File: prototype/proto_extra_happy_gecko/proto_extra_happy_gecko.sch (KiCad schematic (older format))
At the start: 0 parts

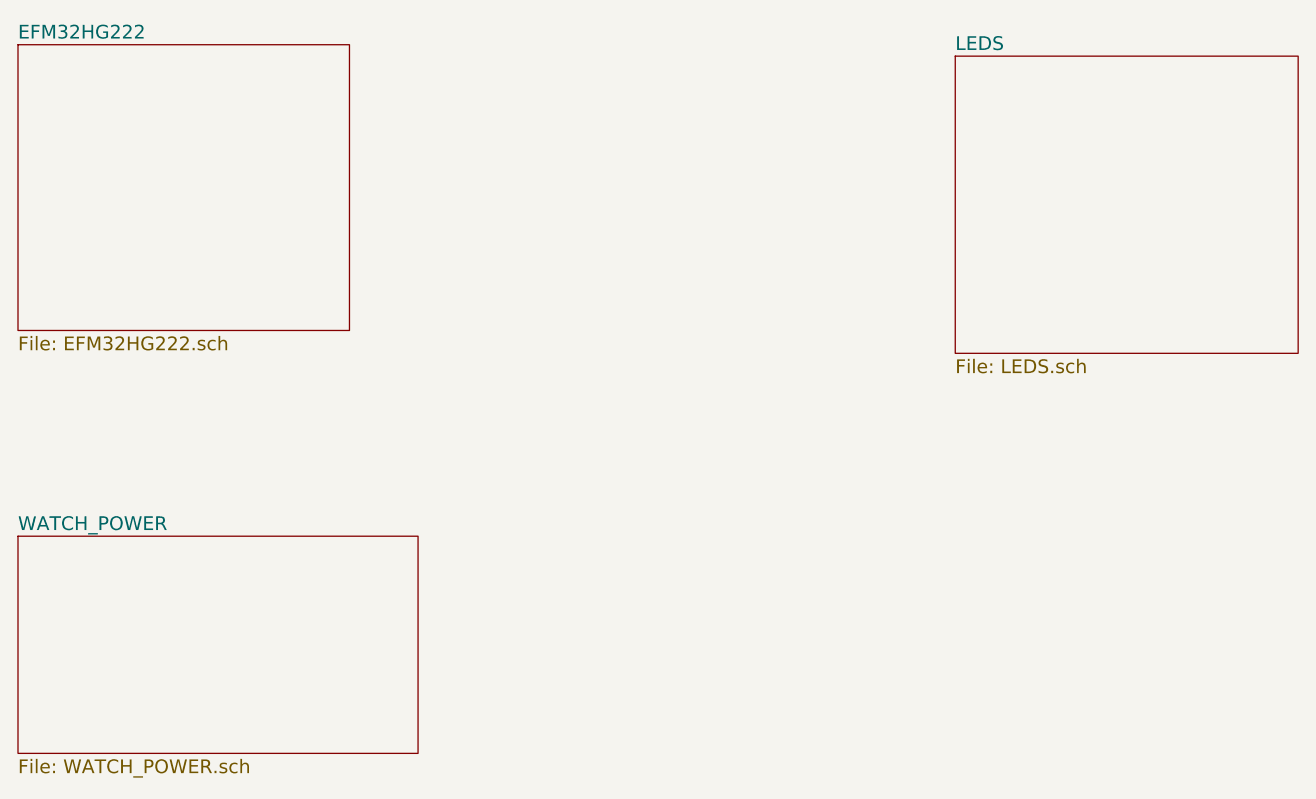
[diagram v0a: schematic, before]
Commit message: Added all leds, 3.3Vreg, and routed busses
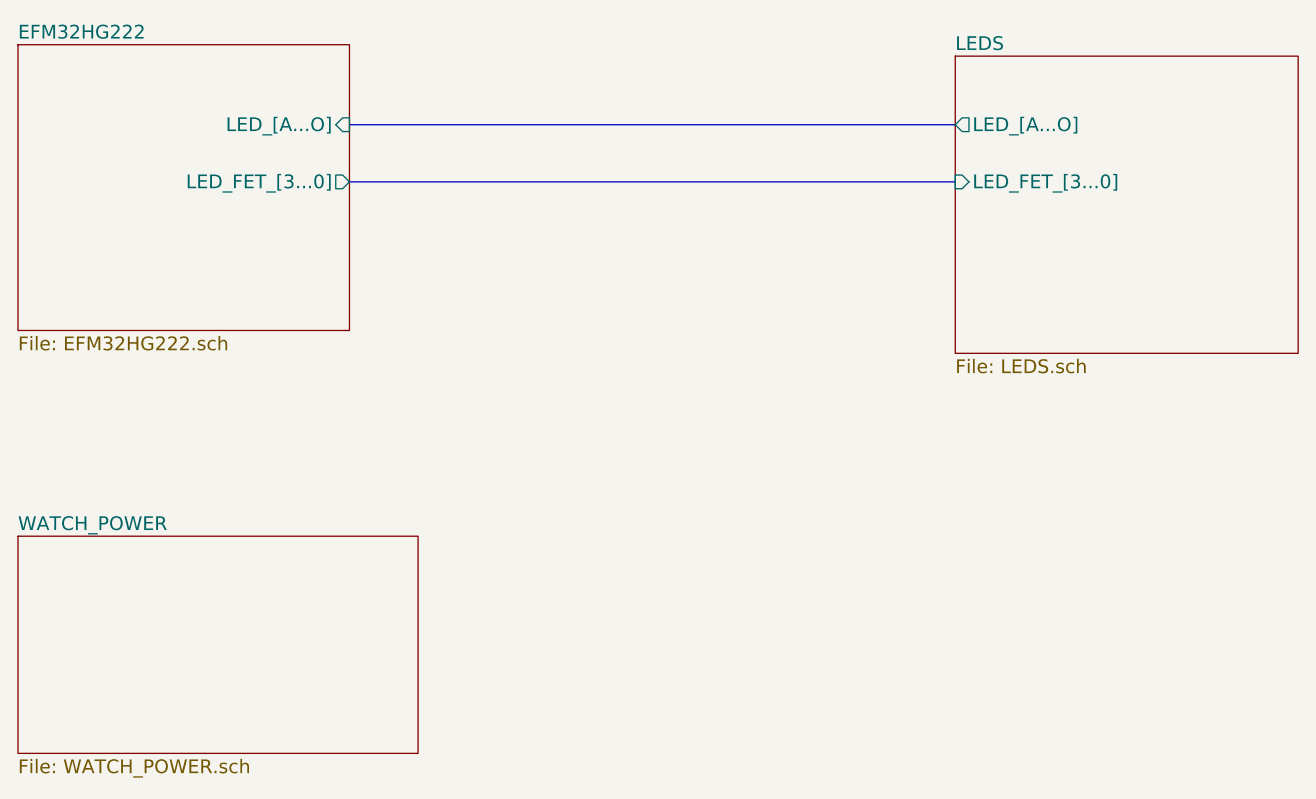
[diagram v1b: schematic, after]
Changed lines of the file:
@@
 LIBS:xtal
 LIBS:capacitors
-LIBS:inductor
 LIBS:mosfet
 LIBS:led
 LIBS:resistor
+LIBS:TLC5954
+LIBS:watch_led
+LIBS:watch_pmos
+LIBS:inductor
+LIBS:regulators
 LIBS:proto_extra_happy_gecko-cache
 EELAYER 25 0
@@
 F0 "EFM32HG222" 60
 F1 "EFM32HG222.sch" 60
-$EndSheet
-$Sheet
-S 6800 2050 1500 1300
-U 58E12669
-F0 "LEDS" 60
-F1 "LEDS.sch" 60
+F2 "LED_FET_[3...0]" O R 4150 2600 60
+F3 "LED_[A...O]" I R 4150 2350 60
 $EndSheet
 $Sheet
@@
 F1 "WATCH_POWER.sch" 60
 $EndSheet
+$Sheet
+S 6800 2050 1500 1300
+U 58E12669
+F0 "LEDS" 60
+F1 "LEDS.sch" 60
+F2 "LED_[A...O]" O L 6800 2350 60
+F3 "LED_FET_[3...0]" I L 6800 2600 60
+$EndSheet
+Wire Bus Line
+	6800 2350 4150 2350
+Wire Bus Line
+	4150 2600 6800 2600
 $EndSCHEMATC
